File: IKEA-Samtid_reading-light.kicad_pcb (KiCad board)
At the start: 2 copper layers, 21 x 100 mm, 31 parts, among them IC1 ATTINY25-S, P1 CONN_2, U1 MCP1804-SOT23-5, U2 PT4115-SOT89-5

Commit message: Fixed wrong 5V regulator footprint. SOT23-5 was needed, used SOT23-6 :-(
Quick fix for prev. boards: solder-bridge from pin #6 to pin #5 (SOT23-6 footprint).
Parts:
- U1: footprint my_parts:MADW__SOT23-6 -> my_parts:MADW__SOT23-5
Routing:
- net +5V: track 105.3 -> 104.2 mm
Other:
- board text added: "2014 - blog.spitzenpfeil.org Reading-light I**A S*mt*d V0.10.b"
- board text removed: "2014 - blog.spitzenpfeil.org Reading-light I**A S*mt*d V0.10.a"

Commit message: Added a safety warning to silkscreen. This board gets quite hot.
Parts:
- added G***: fire_silkscreen-back_6mm, fire:fire_silkscreen-back_6mm, B.Cu at (70.4, 88.7)
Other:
- board text added: "2014 - blog.spitzenpfeil.org Reading-light I**A S*mt*d V0.10.c"
- board text added: "Only use in well ventilated areas. Keep away from easily combustible material."
- board text removed: "2014 - blog.spitzenpfeil.org Reading-light I**A S*mt*d V0.10.b"

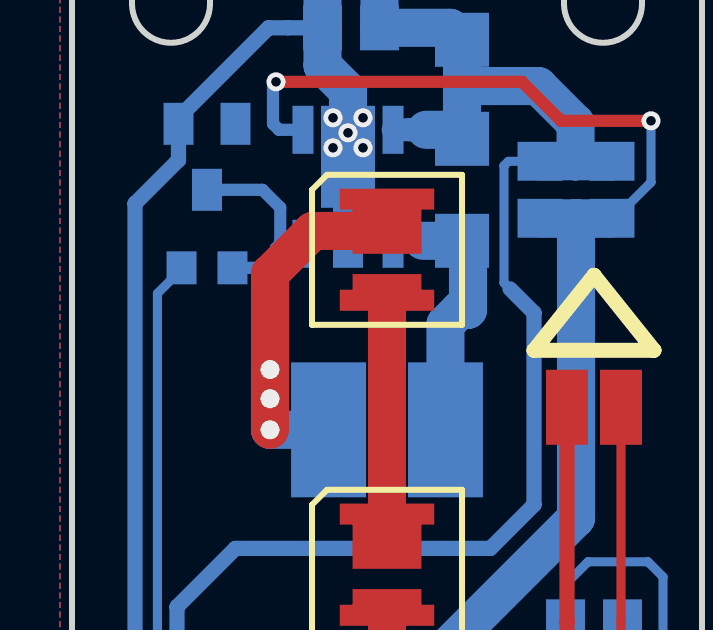
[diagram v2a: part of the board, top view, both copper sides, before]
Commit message: Tweaks.
1) C6: 100nF --> 22nF (faster response to finger touch). RC < 100ms.
2) Added 10k pull-down for _dim on PT4115 to prevent / reduce LED flash on power-up.
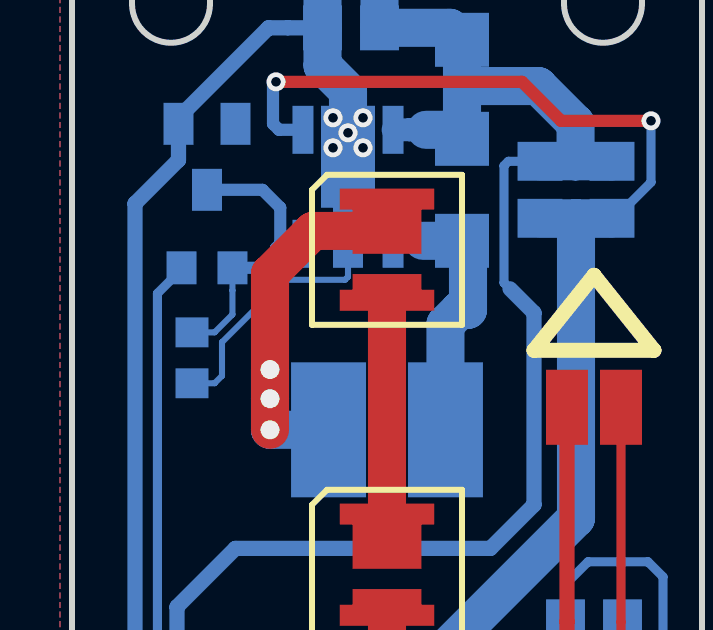
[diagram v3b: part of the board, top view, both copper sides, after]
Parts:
- added R2: 10k, my_parts:MADW__R0603_2, B.Cu at (64.5, 65.6)
- C6: value 100nF -> 22nF
- R_FS1, R_FS2: value 10M -> 4.7M
- renumbered G*** to LOGO3, R2 to R1
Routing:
- net GNDPWR: track 70.0 -> 78.7 mm
- net /_dim: track 6.64 -> 9.79 mm
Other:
- board text added: "2014 - blog.spitzenpfeil.org Reading-light I**A S*mt*d V0.11.a"
- board text removed: "2014 - blog.spitzenpfeil.org Reading-light I**A S*mt*d V0.10.c"

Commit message: Silkscreen tweaks.
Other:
- board text added: "2014 - blog.spitzenpfeil.org Reading-light I**A S*mt*d V0.11.b"
- board text removed: "2014 - blog.spitzenpfeil.org Reading-light I**A S*mt*d V0.11.a"
